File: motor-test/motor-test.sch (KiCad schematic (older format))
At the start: 34 parts, among them J1 Conn_01x06_Male, J2 Conn_01x02_Male, J3 Conn_01x02_Male, Q1 MMBT3904, SW1 SW_DIP_x08, U2 TBD62783AFNGEL, U3 TBD62083AFNGEL, U4 X7WBX

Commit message: design review changes fix VCC and GND swap on high side driver simplify catch diode setup to 1 diode schematic cleanup correct dV/dt cap value to give 2 ms soft start increase triac trigger current to 4.3 mA add manufacturer part numbers and data sheet link on some parts
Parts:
- removed D4: S1GTR, Diode_SMD:D_SMA, symbol Device:D
- C6: value 100 nF -> 1 nF
- D2: value Q_TRIAC_A1A2G -> Z0103MN0
- J1: value Conn_01x06_Male -> DF3_6
- J2, J3: value Conn_01x02_Male -> DF3_2
- R1: value 2.2 k -> 1 k
- S1: value TTWY4 -> 147873-1; footprint PB_3.5x6 -> kicad_pcb:PB_3.5x6
- SW1: value SW_DIP_x08 -> 208-8
- U4: value X7WBX -> DPS1133FIA-13
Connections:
- net +24V: now also D1.1 (K)
- net CB_OUT: no longer D1.1 (K)
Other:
- moved on the sheet: Q1, R1, S1
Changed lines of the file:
@@
 EESchema Schematic File Version 4
+LIBS:motor-test-cache
 EELAYER 29 0
 EELAYER END
@@
 P 5950 2400
 F 0 "D2" V 6216 2400 50  0000 C CNN
-F 1 "Q_TRIAC_A1A2G" V 6125 2400 50  0000 C CNN
+F 1 "Z0103MN0" V 6125 2400 50  0000 C CNN
 F 2 "Package_TO_SOT_SMD:SOT-223-3_TabPin2" V 6025 2425 50  0001 C CNN
 F 3 "http://www.ween-semi.com/sites/default/files/2018-10/z0103mn0.pdf" V 5950 2400 50  0001 C CNN
@@
 	7000 2400 6300 2400
 Wire Wire Line
-	5850 2550 5850 3100
+	5850 2550 5850 4100
 $Comp
 L power:GND #PWR0104
 U 1 1 5D2FC8E3
-P 5850 3800
-F 0 "#PWR0104" H 5850 3550 50  0001 C CNN
-F 1 "GND" H 5855 3627 50  0000 C CNN
-F 2 "" H 5850 3800 50  0001 C CNN
-F 3 "" H 5850 3800 50  0001 C CNN
-	1    5850 3800
+P 5850 4800
+F 0 "#PWR0104" H 5850 4550 50  0001 C CNN
+F 1 "GND" H 5855 4627 50  0000 C CNN
+F 2 "" H 5850 4800 50  0001 C CNN
+F 3 "" H 5850 4800 50  0001 C CNN
+	1    5850 4800
 	1    0    0    -1
 $EndComp
@@
 L Device:R R1
 U 1 1 5D2FCF20
-P 5850 3650
-F 0 "R1" H 5920 3696 50  0000 L CNN
-F 1 "2.2 k" H 5920 3605 50  0000 L CNN
-F 2 "kicad_pcb:R_0603_1608Metric" V 5780 3650 50  0001 C CNN
-F 3 "~" H 5850 3650 50  0001 C CNN
-	1    5850 3650
-	1    0    0    -1
-$EndComp
-Wire Wire Line
-	5550 3300 5050 3300
-Text Label 5050 3300 0    50   ~ 0
+P 5850 4650
+F 0 "R1" H 5920 4696 50  0000 L CNN
+F 1 "1 k" H 5920 4605 50  0000 L CNN
+F 2 "kicad_pcb:R_0603_1608Metric" V 5780 4650 50  0001 C CNN
+F 3 "~" H 5850 4650 50  0001 C CNN
+	1    5850 4650
+	1    0    0    -1
+$EndComp
+Wire Wire Line
+	5550 4300 5450 4300
+Text Label 5450 4250 1    50   ~ 0
 TRIAC0
 Text Label 5850 2950 1    50   ~ 0
@@
 L Device:Q_NPN_BEC Q1
 U 1 1 5D2FC06A
-P 5750 3300
-F 0 "Q1" H 5940 3346 50  0000 L CNN
-F 1 "MMBT3904" H 5940 3255 50  0000 L CNN
-F 2 "kicad_pcb:SOT-23" H 5950 3400 50  0001 C CNN
-F 3 "~" H 5750 3300 50  0001 C CNN
-	1    5750 3300
+P 5750 4300
+F 0 "Q1" H 5940 4346 50  0000 L CNN
+F 1 "MMBT3904" H 5940 4255 50  0000 L CNN
+F 2 "kicad_pcb:SOT-23" H 5950 4400 50  0001 C CNN
+F 3 "~" H 5750 4300 50  0001 C CNN
+	1    5750 4300
 	1    0    0    -1
 $EndComp
@@
 Wire Wire Line
 	6250 2400 6100 2400
-Wire Wire Line
-	5800 2400 5550 2400
-Wire Wire Line
-	5550 2400 5550 2000
-Wire Wire Line
-	5550 2000 5800 2000
 $Comp
 L capacitors:capacitor_0805 C1
@@
 	1    0    0    -1
 $EndComp
-Wire Wire Line
-	5550 2400 5350 2400
-Connection ~ 5550 2400
 $Comp
 L ic:X7WBX U4
@@
 P 3100 2300
 F 0 "U4" H 3425 2465 50  0000 C CNN
-F 1 "X7WBX" H 3425 2374 50  0000 C CNN
+F 1 "DPS1133FIA-13" H 3425 2374 50  0000 C CNN
 F 2 "kicad_pcb:QFN-17-Diodes1" H 3100 2350 50  0001 L CNN
-F 3 "$PARTS/X7WBX/DPS1133.pdf" V 3350 2300 50  0001 C CNN
+F 3 "https://www.diodes.com/assets/Datasheets/DPS1133.pdf" V 3350 2300 50  0001 C CNN
 	1    3100 2300
 	1    0    0    -1
@@
 	1    0    0    -1
 $EndComp
-Wire Wire Line
-	3000 2400 2950 2400
 $Comp
 L Device:LED D3
@@
 Wire Wire Line
 	4900 3600 4900 3550
-Wire Wire Line
-	3850 2400 3900 2400
 Connection ~ 5350 2400
 $Comp
@@
 	2950 2600 3000 2600
 Connection ~ 2950 2700
-Wire Wire Line
-	3000 2500 2750 2500
-Wire Wire Line
-	2750 2500 2750 2100
-Wire Wire Line
-	2750 2100 2500 2100
 $Comp
 L capacitors:capacitor_0805 C7
@@
 P 3900 3250
 F 0 "C6" V 3750 3200 50  0000 L CNN
-F 1 "100 nF" V 4050 3100 50  0000 L CNN
+F 1 "1 nF" V 4050 3100 50  0000 L CNN
 F 2 "kicad_pcb:C_0603_1608Metric" V 3900 3250 50  0001 C CNN
 F 3 "" H 3900 3250 50  0000 C CNN
@@
 P 1200 6700
 F 0 "SW1" H 1200 7367 50  0000 C CNN
-F 1 "SW_DIP_x08" H 1200 7276 50  0000 C CNN
+F 1 "208-8" H 1200 7276 50  0000 C CNN
 F 2 "Package_DIP:DIP-16_W7.62mm" H 1200 6700 50  0001 C CNN
 F 3 "~" H 1200 6700 50  0001 C CNN
@@
 	1    0    0    -1
 $EndComp
-Text Label 2500 2100 0    50   ~ 0
+Text Label 2600 2500 0    50   ~ 0
 CB_EN
 Wire Wire Line
@@
 P 8500 2700
 F 0 "J1" H 8472 2674 50  0000 R CNN
-F 1 "Conn_01x06_Male" H 8472 2583 50  0000 R CNN
+F 1 "DF3_6" H 8472 2583 50  0000 R CNN
 F 2 "kicad_pcb:DF3_6" H 8500 2700 50  0001 C CNN
 F 3 "~" H 8500 2700 50  0001 C CNN
@@
 P 950 2400
 F 0 "J2" H 1058 2581 50  0000 C CNN
-F 1 "Conn_01x02_Male" H 1058 2490 50  0000 C CNN
+F 1 "DF3_2" H 1058 2490 50  0000 C CNN
 F 2 "kicad_pcb:DF3_2" H 950 2400 50  0001 C CNN
 F 3 "~" H 950 2400 50  0001 C CNN
@@
 P 950 1500
 F 0 "J3" H 1058 1681 50  0000 C CNN
-F 1 "Conn_01x02_Male" H 1058 1590 50  0000 C CNN
+F 1 "DF3_2" H 1058 1590 50  0000 C CNN
 F 2 "kicad_pcb:DF3_2" H 950 1500 50  0001 C CNN
 F 3 "~" H 950 1500 50  0001 C CNN
@@
 L misc:TTWY4 S1
 U 1 1 5D629DA3
-P 4950 1750
-F 0 "S1" V 4950 1606 50  0000 R CNN
-F 1 "TTWY4" H 4950 1600 50  0001 L BNN
-F 2 "PB_3.5x6" H 4950 1750 50  0001 C CNN
-F 3 "" H 4950 1750 50  0001 C CNN
-	1    4950 1750
+P 5350 3650
+F 0 "S1" V 5350 3506 50  0000 R CNN
+F 1 "147873-1" H 5350 3500 50  0001 L BNN
+F 2 "kicad_pcb:PB_3.5x6" H 5350 3650 50  0001 C CNN
+F 3 "" H 5350 3650 50  0001 C CNN
+	1    5350 3650
 	0    -1   -1   0
 $EndComp
@@
 L combined:+5V #PWR0121
 U 1 1 5D62D05E
-P 5050 1500
-F 0 "#PWR0121" H 5050 1590 50  0001 C CNN
-F 1 "+5V" H 5046 1643 50  0000 C CNN
-F 2 "" H 5050 1500 50  0000 C CNN
-F 3 "" H 5050 1500 50  0000 C CNN
-	1    5050 1500
-	1    0    0    -1
-$EndComp
-Wire Wire Line
-	5050 2000 5050 3300
-$Comp
-L Device:D D4
-U 1 1 5D63CADC
-P 3400 1950
-F 0 "D4" H 3400 2166 50  0000 C CNN
-F 1 "S1GTR" H 3400 2075 50  0000 C CNN
-F 2 "Diode_SMD:D_SMA" H 3400 1950 50  0001 C CNN
-F 3 "http://www.smc-diodes.com/propdf/S1A-S1M%20N0560%20REV.B.pdf" H 3400 1950 50  0001 C CNN
-	1    3400 1950
-	1    0    0    -1
-$EndComp
-Wire Wire Line
-	3550 1950 3900 1950
-Wire Wire Line
-	3900 1950 3900 2400
-Connection ~ 3900 2400
-Wire Wire Line
-	3900 2400 5350 2400
-Wire Wire Line
-	3250 1950 2950 1950
-Wire Wire Line
-	2950 1950 2950 2400
-Connection ~ 2950 2400
-Wire Wire Line
-	2950 2400 2250 2400
+P 5450 3400
+F 0 "#PWR0121" H 5450 3490 50  0001 C CNN
+F 1 "+5V" H 5446 3543 50  0000 C CNN
+F 2 "" H 5450 3400 50  0000 C CNN
+F 3 "" H 5450 3400 50  0000 C CNN
+	1    5450 3400
+	1    0    0    -1
+$EndComp
 NoConn ~ 1500 6300
 $Comp
@@
 	-1   0    0    1
 $EndComp
+Wire Wire Line
+	5350 2400 5800 2400
+Wire Wire Line
+	3850 2400 5350 2400
+Wire Wire Line
+	2250 2400 3000 2400
+$Comp
+L power:+24V #PWR0124
+U 1 1 5D302241
+P 5800 2000
+F 0 "#PWR0124" H 5800 1850 50  0001 C CNN
+F 1 "+24V" H 5815 2173 50  0000 C CNN
+F 2 "" H 5800 2000 50  0001 C CNN
+F 3 "" H 5800 2000 50  0001 C CNN
+	1    5800 2000
+	0    -1   -1   0
+$EndComp
+Wire Wire Line
+	5450 3900 5450 4300
+Wire Wire Line
+	2600 2500 3000 2500
 $EndSCHEMATC

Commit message: change component values to available ones
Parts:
- C2: value 100 nF -> 10 nF
- R10, R11, R12, R7, R8, R9: value 5.1 k -> DNP
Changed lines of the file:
@@
 P 6300 2600
 F 0 "C2" H 6435 2646 50  0000 L CNN
-F 1 "100 nF" H 6435 2555 50  0000 L CNN
+F 1 "10 nF" H 6435 2555 50  0000 L CNN
 F 2 "kicad_pcb:C_0603_1608Metric" V 6300 2600 50  0001 C CNN
 F 3 "" H 6300 2600 50  0000 C CNN
@@
 P 1950 7200
 F 0 "R7" H 2020 7246 50  0000 L CNN
-F 1 "5.1 k" H 2020 7155 50  0000 L CNN
+F 1 "DNP" H 2020 7155 50  0000 L CNN
 F 2 "kicad_pcb:R_0603_1608Metric" V 1880 7200 50  0001 C CNN
 F 3 "~" H 1950 7200 50  0001 C CNN
@@
 P 2300 7200
 F 0 "R8" H 2370 7246 50  0000 L CNN
-F 1 "5.1 k" H 2370 7155 50  0000 L CNN
+F 1 "DNP" H 2370 7155 50  0000 L CNN
 F 2 "kicad_pcb:R_0603_1608Metric" V 2230 7200 50  0001 C CNN
 F 3 "~" H 2300 7200 50  0001 C CNN
@@
 P 2650 7200
 F 0 "R9" H 2720 7246 50  0000 L CNN
-F 1 "5.1 k" H 2720 7155 50  0000 L CNN
+F 1 "DNP" H 2720 7155 50  0000 L CNN
 F 2 "kicad_pcb:R_0603_1608Metric" V 2580 7200 50  0001 C CNN
 F 3 "~" H 2650 7200 50  0001 C CNN
@@
 P 3000 7200
 F 0 "R10" H 3070 7246 50  0000 L CNN
-F 1 "5.1 k" H 3070 7155 50  0000 L CNN
+F 1 "DNP" H 3070 7155 50  0000 L CNN
 F 2 "kicad_pcb:R_0603_1608Metric" V 2930 7200 50  0001 C CNN
 F 3 "~" H 3000 7200 50  0001 C CNN
@@
 P 3350 7200
 F 0 "R11" H 3420 7246 50  0000 L CNN
-F 1 "5.1 k" H 3420 7155 50  0000 L CNN
+F 1 "DNP" H 3420 7155 50  0000 L CNN
 F 2 "kicad_pcb:R_0603_1608Metric" V 3280 7200 50  0001 C CNN
 F 3 "~" H 3350 7200 50  0001 C CNN
@@
 P 3700 7200
 F 0 "R12" H 3770 7246 50  0000 L CNN
-F 1 "5.1 k" H 3770 7155 50  0000 L CNN
+F 1 "DNP" H 3770 7155 50  0000 L CNN
 F 2 "kicad_pcb:R_0603_1608Metric" V 3630 7200 50  0001 C CNN
 F 3 "~" H 3700 7200 50  0001 C CNN

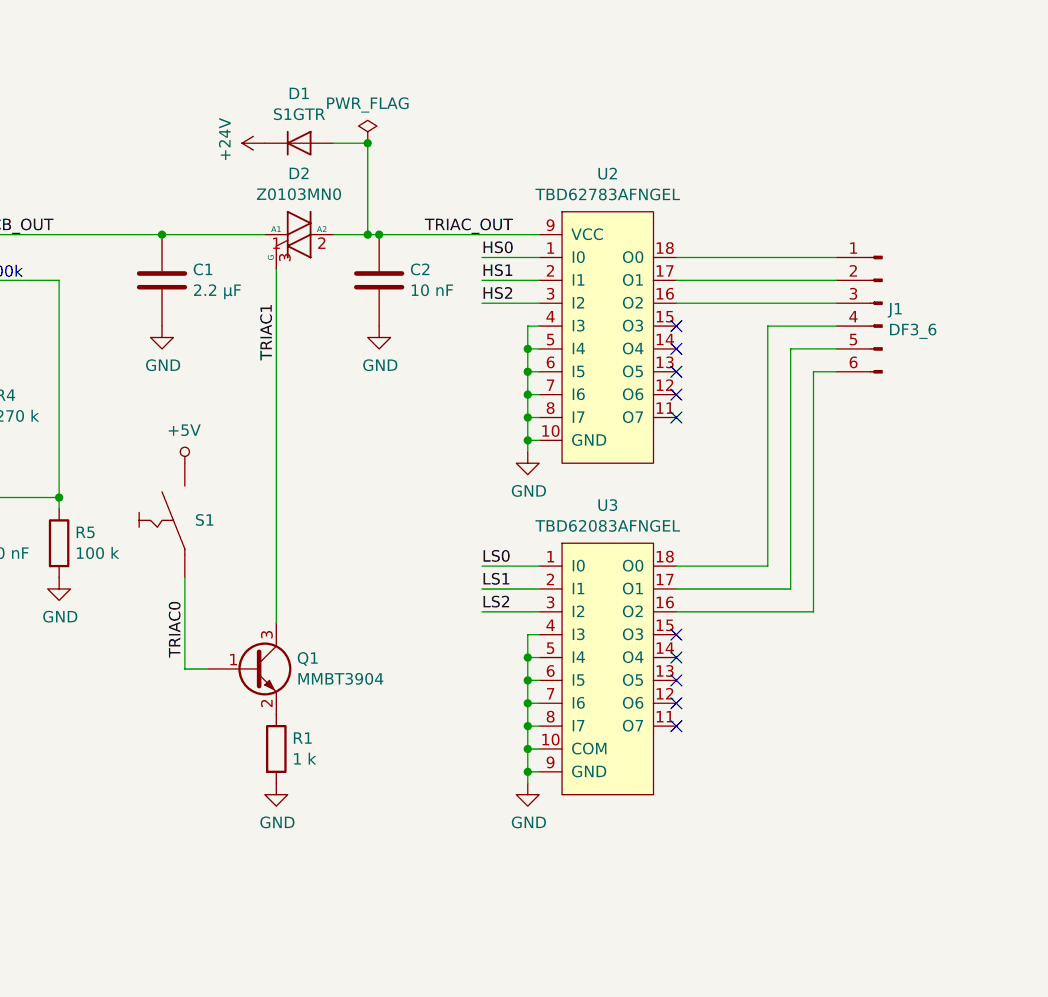
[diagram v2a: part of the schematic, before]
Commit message: fix for motor not stopping due to the gate pull up resistor current in the high side driver, the triac was not turning off.
Cut and dead bugged a triac based low side driver as shown in the schematic.
This will use 8 triacs for the low side.

Staying with triacs, but SCRs would work.
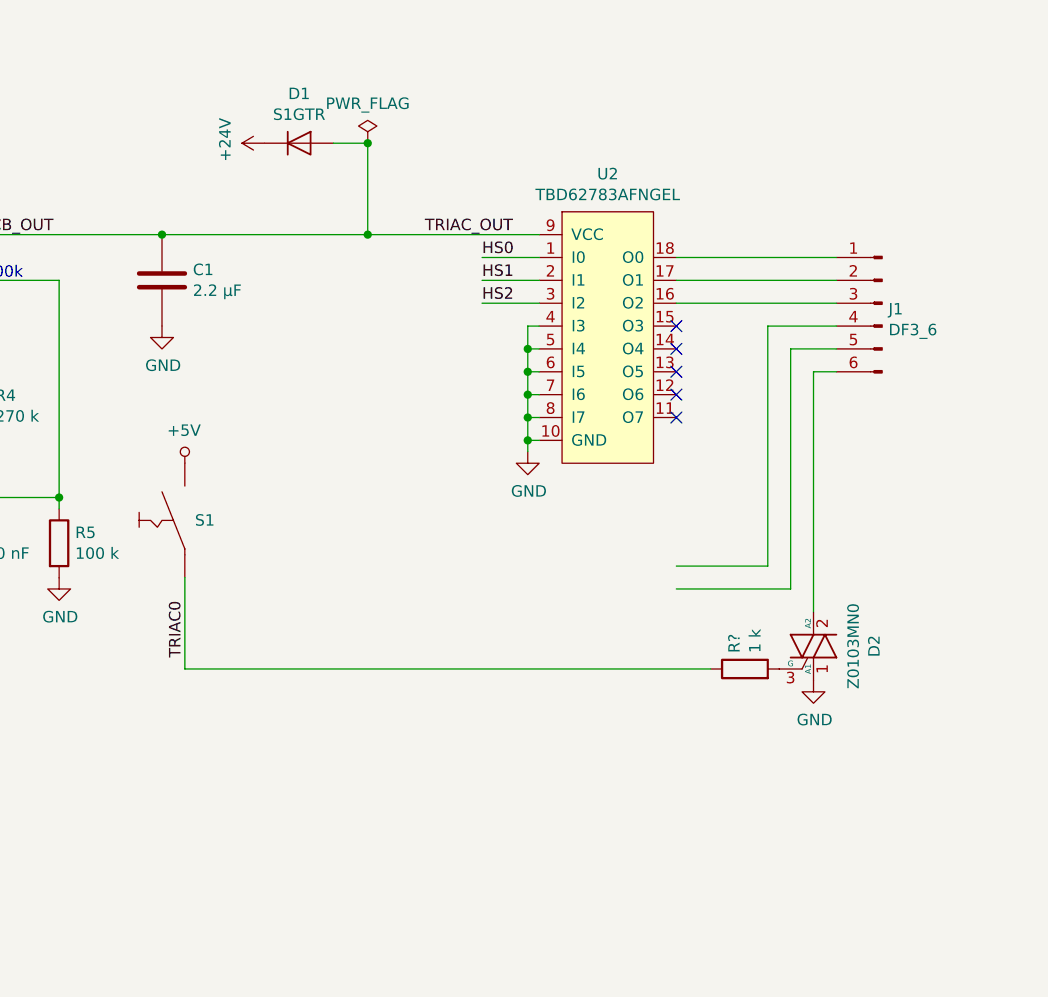
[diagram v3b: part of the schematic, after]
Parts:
- removed C2: 10 nF, kicad_pcb:C_0603_1608Metric, symbol capacitors:capacitor_0805
- removed Q1: MMBT3904, kicad_pcb:SOT-23, symbol Device:Q_NPN_BEC
- removed R1: 1 k, kicad_pcb:R_0603_1608Metric, symbol Device:R
- removed U3: TBD62083AFNGEL, motor-test:SSOP-18_4.4x6.5mm_P0.65mm, symbol motor-test:TBD62083AFNGEL
- added R?: 1 k, kicad_pcb:R_0603_1608Metric, symbol Device:R
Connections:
- net CB_OUT: now also D1.2 (A), U2.9 (VCC); no longer D2.1 (A1)
- net GND: now also D2.1 (A1)
- net TRIAC0: now also R?.1
- net at J1.6 (Pin_6): now also D2.2 (A2)
- net TRIAC1: no longer names the net of D2.3 (G)
- net TRIAC1: now also R?.2
- removed net TRIAC_OUT: D1.2 (A), D2.2 (A2), U2.9 (VCC)
- no-connect marks 11 -> 6
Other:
- moved on the sheet: D2
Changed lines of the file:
@@
 $EndDescr
-$Comp
-L motor-test:TBD62083AFNGEL U3
-U 1 1 5D2EACE2
-P 7300 4300
-F 0 "U3" H 7300 5015 50  0000 C CNN
-F 1 "TBD62083AFNGEL" H 7300 4924 50  0000 C CNN
-F 2 "motor-test:SSOP-18_4.4x6.5mm_P0.65mm" H 7300 4850 50  0001 C CNN
-F 3 "https://toshiba.semicon-storage.com/info/docget.jsp?did=29893&prodName=TBD62083AFG" H 7300 4850 50  0001 C CNN
-	1    7300 4300
-	1    0    0    -1
-$EndComp
 $Comp
 L motor-test:TBD62783AFNGEL U2
@@
 $EndComp
 $Comp
-L power:GND #PWR0101
-U 1 1 5D2EDC96
-P 6950 4800
-F 0 "#PWR0101" H 6950 4550 50  0001 C CNN
-F 1 "GND" H 6955 4627 50  0000 C CNN
-F 2 "" H 6950 4800 50  0001 C CNN
-F 3 "" H 6950 4800 50  0001 C CNN
-	1    6950 4800
-	1    0    0    -1
-$EndComp
-Wire Wire Line
-	7000 4650 6950 4650
-Wire Wire Line
-	6950 4650 6950 4750
-Wire Wire Line
-	7000 4750 6950 4750
-Connection ~ 6950 4750
-Wire Wire Line
-	6950 4750 6950 4800
-$Comp
 L power:GND #PWR0102
 U 1 1 5D2EED3C
@@
 L Device:Q_TRIAC_A1A2G D2
 U 1 1 5D2F6EF9
-P 5950 2400
-F 0 "D2" V 6216 2400 50  0000 C CNN
-F 1 "Z0103MN0" V 6125 2400 50  0000 C CNN
-F 2 "Package_TO_SOT_SMD:SOT-223-3_TabPin2" V 6025 2425 50  0001 C CNN
-F 3 "http://www.ween-semi.com/sites/default/files/2018-10/z0103mn0.pdf" V 5950 2400 50  0001 C CNN
-	1    5950 2400
-	0    1    -1   0
-$EndComp
-Wire Wire Line
-	7000 2400 6300 2400
-Wire Wire Line
-	5850 2550 5850 4100
-$Comp
-L power:GND #PWR0104
-U 1 1 5D2FC8E3
-P 5850 4800
-F 0 "#PWR0104" H 5850 4550 50  0001 C CNN
-F 1 "GND" H 5855 4627 50  0000 C CNN
-F 2 "" H 5850 4800 50  0001 C CNN
-F 3 "" H 5850 4800 50  0001 C CNN
-	1    5850 4800
-	1    0    0    -1
-$EndComp
-$Comp
-L Device:R R1
-U 1 1 5D2FCF20
-P 5850 4650
-F 0 "R1" H 5920 4696 50  0000 L CNN
-F 1 "1 k" H 5920 4605 50  0000 L CNN
-F 2 "kicad_pcb:R_0603_1608Metric" V 5780 4650 50  0001 C CNN
-F 3 "~" H 5850 4650 50  0001 C CNN
-	1    5850 4650
-	1    0    0    -1
-$EndComp
-Wire Wire Line
-	5550 4300 5450 4300
+P 8200 4200
+F 0 "D2" V 8466 4200 50  0000 C CNN
+F 1 "Z0103MN0" V 8375 4200 50  0000 C CNN
+F 2 "Package_TO_SOT_SMD:SOT-223-3_TabPin2" V 8275 4225 50  0001 C CNN
+F 3 "http://www.ween-semi.com/sites/default/files/2018-10/z0103mn0.pdf" V 8200 4200 50  0001 C CNN
+	1    8200 4200
+	1    0    0    -1
+$EndComp
 Text Label 5450 4250 1    50   ~ 0
 TRIAC0
-Text Label 5850 2950 1    50   ~ 0
-TRIAC1
-$Comp
-L capacitors:capacitor_0805 C2
-U 1 1 5D3005C5
-P 6300 2600
-F 0 "C2" H 6435 2646 50  0000 L CNN
-F 1 "10 nF" H 6435 2555 50  0000 L CNN
-F 2 "kicad_pcb:C_0603_1608Metric" V 6300 2600 50  0001 C CNN
-F 3 "" H 6300 2600 50  0000 C CNN
-	1    6300 2600
-	1    0    0    -1
-$EndComp
-Connection ~ 6300 2400
-Wire Wire Line
-	6300 2400 6250 2400
-$Comp
-L power:GND #PWR0105
-U 1 1 5D300B40
-P 6300 2800
-F 0 "#PWR0105" H 6300 2550 50  0001 C CNN
-F 1 "GND" H 6305 2627 50  0000 C CNN
-F 2 "" H 6300 2800 50  0001 C CNN
-F 3 "" H 6300 2800 50  0001 C CNN
-	1    6300 2800
-	1    0    0    -1
-$EndComp
-$Comp
-L Device:Q_NPN_BEC Q1
-U 1 1 5D2FC06A
-P 5750 4300
-F 0 "Q1" H 5940 4346 50  0000 L CNN
-F 1 "MMBT3904" H 5940 4255 50  0000 L CNN
-F 2 "kicad_pcb:SOT-23" H 5950 4400 50  0001 C CNN
-F 3 "~" H 5750 4300 50  0001 C CNN
-	1    5750 4300
-	1    0    0    -1
-$EndComp
 $Comp
 L Device:D D1
@@
 	6250 2000 6250 2400
 Connection ~ 6250 2400
-Wire Wire Line
-	6250 2400 6100 2400
 $Comp
 L capacitors:capacitor_0805 C1
@@
 CB_EN
 Wire Wire Line
-	7000 4150 6950 4150
-Wire Wire Line
-	6950 4150 6950 4250
-Connection ~ 6950 4650
-Wire Wire Line
-	7000 4550 6950 4550
-Connection ~ 6950 4550
-Wire Wire Line
-	6950 4550 6950 4650
-Wire Wire Line
-	7000 4450 6950 4450
-Connection ~ 6950 4450
-Wire Wire Line
-	6950 4450 6950 4550
-Wire Wire Line
-	7000 4350 6950 4350
-Connection ~ 6950 4350
-Wire Wire Line
-	6950 4350 6950 4450
-Wire Wire Line
-	7000 4250 6950 4250
-Connection ~ 6950 4250
-Wire Wire Line
-	6950 4250 6950 4350
-Wire Wire Line
 	7000 2800 6950 2800
 Wire Wire Line
@@
 Wire Wire Line
 	7000 2700 6750 2700
-Text Label 6750 3850 0    50   ~ 0
-LS0
-Wire Wire Line
-	7000 3850 6750 3850
-Text Label 6750 3950 0    50   ~ 0
-LS1
-Wire Wire Line
-	7000 3950 6750 3950
-Text Label 6750 4050 0    50   ~ 0
-LS2
-Wire Wire Line
-	7000 4050 6750 4050
 Wire Wire Line
 	1500 6700 2650 6700
@@
 	8100 3950 7600 3950
 Wire Wire Line
-	7600 4050 8200 4050
-Wire Wire Line
 	8200 4050 8200 3000
 Wire Wire Line
@@
 NoConn ~ 7600 3100
 NoConn ~ 7600 3200
-NoConn ~ 7600 4150
-NoConn ~ 7600 4250
-NoConn ~ 7600 4350
-NoConn ~ 7600 4450
-NoConn ~ 7600 4550
 $Comp
 L misc:tooling_hole TH1
@@
 $EndComp
 Wire Wire Line
-	5350 2400 5800 2400
-Wire Wire Line
 	3850 2400 5350 2400
 Wire Wire Line
@@
 Wire Wire Line
 	2600 2500 3000 2500
+$Comp
+L power:GND #PWR?
+U 1 1 5D429C65
+P 8200 4350
+F 0 "#PWR?" H 8200 4100 50  0001 C CNN
+F 1 "GND" H 8205 4177 50  0000 C CNN
+F 2 "" H 8200 4350 50  0001 C CNN
+F 3 "" H 8200 4350 50  0001 C CNN
+	1    8200 4350
+	1    0    0    -1
+$EndComp
+$Comp
+L Device:R R?
+U 1 1 5D42A8F9
+P 7900 4300
+F 0 "R?" H 7970 4346 50  0000 L CNN
+F 1 "1 k" H 7970 4255 50  0000 L CNN
+F 2 "kicad_pcb:R_0603_1608Metric" V 7830 4300 50  0001 C CNN
+F 3 "~" H 7900 4300 50  0001 C CNN
+	1    7900 4300
+	0    -1   -1   0
+$EndComp
+Wire Wire Line
+	5350 2400 6250 2400
+Wire Wire Line
+	5450 4300 7750 4300
+Wire Wire Line
+	6250 2400 7000 2400
 $EndSCHEMATC
